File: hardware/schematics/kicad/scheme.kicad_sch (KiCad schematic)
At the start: 15 parts

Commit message: modified schematics
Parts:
- removed CONN: Connector to Controller, symbol Connector:Conn_01x04_Pin
- removed CONN: Connector to Plants, symbol Connector:Conn_01x04_Socket
- removed MOSFET: IRLZ44N, Package_TO_SOT_THT:TO-220-3_Vertical, symbol Transistor_FET:IRLZ44N
- removed R1: 10k, symbol Device:R_US
- removed SC1: Solar_Cell, symbol Device:Solar_Cell
- added J1, J2, J3: RJ45, symbol Connector:RJ45
- added RELAY1, RELAY2: ~, symbol Relay:Relay
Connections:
- net 5V: now also D0.8 (VCC), J1.1, J1.2, J2.1, J2.2, J3.1, J3.2, RELAY1. (VCC), RELAY2. (VCC); no longer CP1.1 (Pin_1), CS1.1 (Pin_1), D1.8 (VCC)
- net GND: now also CONTR.10 (GND), CP1.2 (Pin_2), D0.5 (GND), STEP.3 (OUT-), J1.3, J1.4, J2.3, J2.4, J3.3, J3.4, RELAY1. (VCC), RELAY2. (VCC)
- net at D1.6 (A): now also J3.6
- net at D1.7 (B): now also J3.5
- net at CONTR.9 (5V), STEP.1 (OUT+): now also RELAY2. (VCC); no longer D0.8 (VCC)
- net A: now reaches D0.6 (A)
- net A: now also J1.6, J2.6
- net B: now reaches D0.7 (B)
- net B: now also J1.5, J2.5
- net at D1.2 (~{RE}), D1.3 (DE): now also A1.6 (D3); no longer A1.5 (D2)
- net at CONTR.3 (D0): now also RELAY2. (VCC)
- net at A1.30 (VCC): now also CS1.1 (Pin_1), D1.8 (VCC)
- net at A1.7 (D4): now also RELAY1. (VCC)
- new net: CP1.1 (Pin_1), RELAY1. (VCC)
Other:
- moved on the sheet: A1, BAT, CONTR, CP1, CS1, D0, D1, POW, REG, STEP

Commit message: saved schematics & formatted
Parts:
- removed CONTR: WeMos_D1_mini, Module:WEMOS_D1_mini_light, symbol MCU_Module:WeMos_D1_mini
- added A0: Arduino NANO 5V, symbol MCU_Module:Arduino_Nano_Every
- added L1: LED, symbol Device:LED
- added R1: 220R, symbol Device:R_US
- A1: value Pro Mini 3.3V -> Arduino NANO 5V
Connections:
- net 5V: now also A1.30 (VCC), CS1.1 (Pin_1), D1.8 (VCC); no longer A1.17 (RAW)
- net GND: now also A0.29 (GND), A0.4 (GND), R1.2
- net at RELAY2. (VCC), STEP.1 (OUT+): now also A0.30 (VCC)
- net at D0.1 (RO): now also A0.2 (RX1)
- net at D0.2 (~{RE}): now also D0.3 (DE), A0.6 (D3)
- net at D0.4 (DI): now also A0.1 (TX0)
- net at A1.5 (D2): now also L1.2 (A)
- new net: L1.1 (K), R1.1
- new net: A0.5 (D2), RELAY2. (VCC)
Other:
- moved on the sheet: A1, BAT, CP1, CS1, D0, D1, J1, J2, J3, POW, REG, RELAY1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

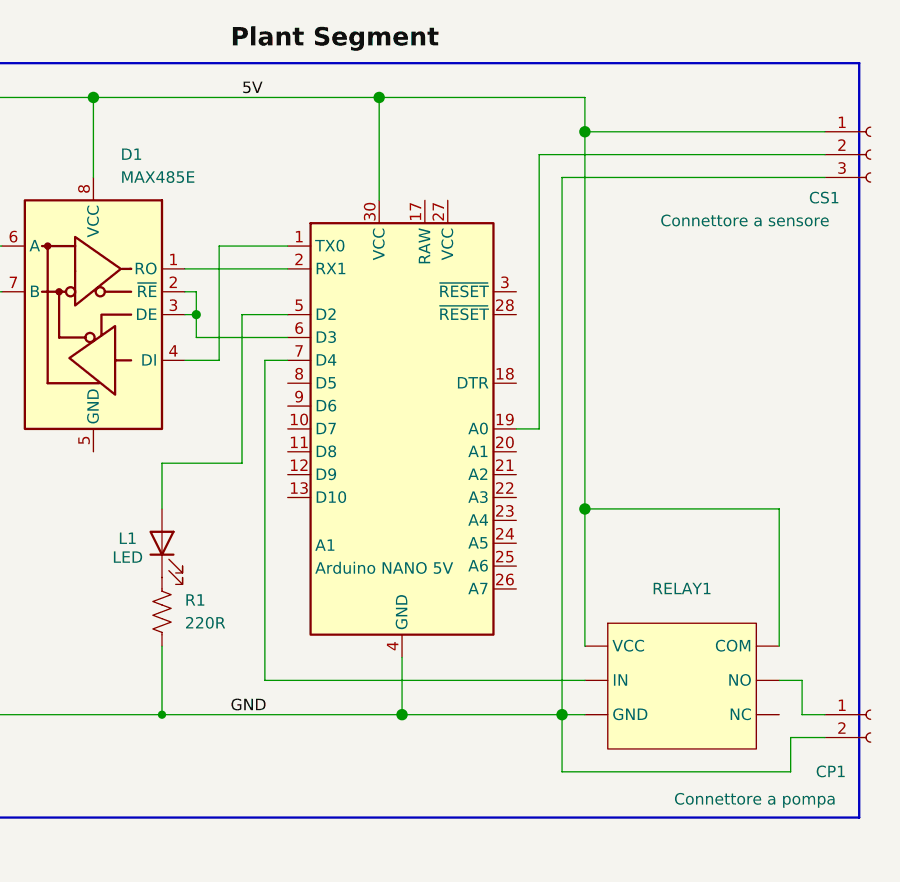
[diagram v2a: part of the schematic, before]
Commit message: Add SaucerSensor class and electrical scheme for plant unit
- Implemented SaucerSensor class with methods to initialize and check if the saucer is full.
- Added initial electrical scheme for the plant unit in KiCad.
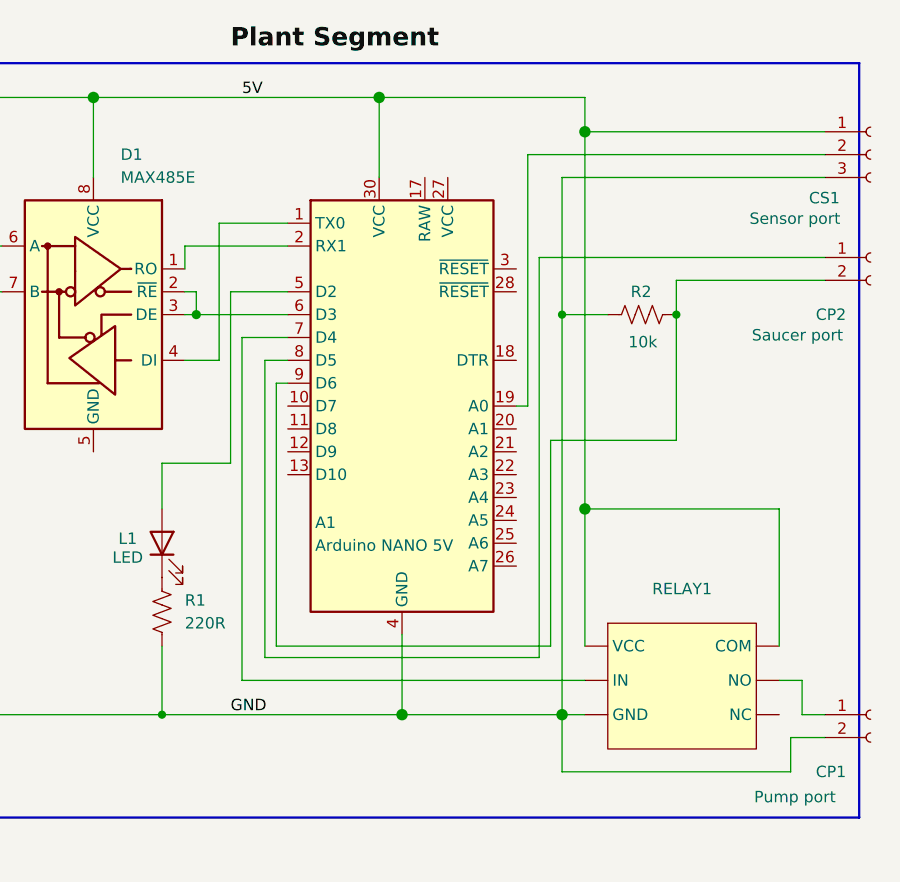
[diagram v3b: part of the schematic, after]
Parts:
- added CP2: Saucer port, symbol Connector:Conn_01x02_Socket
- added R2: 10k, symbol Device:R_US
- CP1: value Connettore a pompa -> Pump port
- CS1: value Connettore a sensore -> Sensor port
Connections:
- net GND: now also R2.1
- net at A1.8 (D5): now also CP2.1 (Pin_1)
- net at A1.9 (D6): now also CP2.2 (Pin_2), R2.2
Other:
- moved on the sheet: A1
